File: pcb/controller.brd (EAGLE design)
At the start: 45 x 45 mm, 22 parts, among them U1 74HCT165TSSOP16

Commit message: update resistor values
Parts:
- C1: value (none) -> 100n
- R1, R2, R3, R4, R5, R6, R7, R8: value (none) -> 4.7k
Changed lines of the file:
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@@
 <attribute name="VALUE" x="32.824" y="0.605" size="0.6096" layer="27" font="vector" ratio="20" rot="R90" align="top-left"/>
 </element>
-<element name="R1" library="rcl" library_urn="urn:adsk.eagle:library:334" package="R0603" package3d_urn="urn:adsk.eagle:package:23555/3" value="" x="32.5" y="42.5" smashed="yes" rot="R45">
+<element name="R1" library="rcl" library_urn="urn:adsk.eagle:library:334" package="R0603" package3d_urn="urn:adsk.eagle:package:23555/3" value="4.7k" x="32.5" y="42.5" smashed="yes" rot="R45">
 <attribute name="NAME" x="31.601971875" y="42.5" size="0.6096" layer="25" rot="R45"/>
 <attribute name="POPULARITY" value="77" x="87.279559375" y="38.009871875" size="1.778" layer="27" rot="R45" display="off"/>
@@
 <attribute name="VALUE" x="33.398025" y="40.703946875" size="1.27" layer="27" rot="R45"/>
 </element>
-<element name="R2" library="rcl" library_urn="urn:adsk.eagle:library:334" package="R0603" package3d_urn="urn:adsk.eagle:package:23555/3" value="" x="25" y="42.5" smashed="yes" rot="R45">
+<element name="R2" library="rcl" library_urn="urn:adsk.eagle:library:334" package="R0603" package3d_urn="urn:adsk.eagle:package:23555/3" value="4.7k" x="25" y="42.5" smashed="yes" rot="R45">
 <attribute name="NAME" x="24.101971875" y="42.5" size="0.6096" layer="25" rot="R45"/>
 <attribute name="POPULARITY" value="77" x="82.4736375" y="40.703946875" size="1.778" layer="27" rot="R45" display="off"/>
@@
 <attribute name="VALUE" x="25.898025" y="40.703946875" size="1.27" layer="27" rot="R45"/>
 </element>
-<element name="R3" library="rcl" library_urn="urn:adsk.eagle:library:334" package="R0603" package3d_urn="urn:adsk.eagle:package:23555/3" value="" x="17.5" y="42.5" smashed="yes" rot="R45">
+<element name="R3" library="rcl" library_urn="urn:adsk.eagle:library:334" package="R0603" package3d_urn="urn:adsk.eagle:package:23555/3" value="4.7k" x="17.5" y="42.5" smashed="yes" rot="R45">
 <attribute name="NAME" x="16.601971875" y="42.5" size="0.6096" layer="25" rot="R45"/>
 <attribute name="POPULARITY" value="77" x="77.667715625" y="43.398025" size="1.778" layer="27" rot="R45" display="off"/>
@@
 <attribute name="VALUE" x="18.398025" y="40.703946875" size="1.27" layer="27" rot="R45"/>
 </element>
-<element name="R4" library="rcl" library_urn="urn:adsk.eagle:library:334" package="R0603" package3d_urn="urn:adsk.eagle:package:23555/3" value="" x="10" y="42.5" smashed="yes" rot="R45">
+<element name="R4" library="rcl" library_urn="urn:adsk.eagle:library:334" package="R0603" package3d_urn="urn:adsk.eagle:package:23555/3" value="4.7k" x="10" y="42.5" smashed="yes" rot="R45">
 <attribute name="NAME" x="9.101971875" y="42.5" size="0.6096" layer="25" rot="R45"/>
 <attribute name="POPULARITY" value="77" x="72.861790625" y="46.0921" size="1.778" layer="27" rot="R45" display="off"/>
@@
 <attribute name="VALUE" x="10.898025" y="40.703946875" size="1.27" layer="27" rot="R45"/>
 </element>
-<element name="R5" library="rcl" library_urn="urn:adsk.eagle:library:334" package="R0603" package3d_urn="urn:adsk.eagle:package:23555/3" value="" x="10" y="27.5" smashed="yes" rot="R45">
+<element name="R5" library="rcl" library_urn="urn:adsk.eagle:library:334" package="R0603" package3d_urn="urn:adsk.eagle:package:23555/3" value="4.7k" x="10" y="27.5" smashed="yes" rot="R45">
 <attribute name="NAME" x="9.101971875" y="27.5" size="0.6096" layer="25" rot="R45"/>
 <attribute name="POPULARITY" value="77" x="75.55586875" y="33.786178125" size="1.778" layer="27" rot="R45" display="off"/>
@@
 <attribute name="VALUE" x="10.898025" y="25.703946875" size="1.27" layer="27" rot="R45"/>
 </element>
-<element name="R6" library="rcl" library_urn="urn:adsk.eagle:library:334" package="R0603" package3d_urn="urn:adsk.eagle:package:23555/3" value="" x="17.5" y="27.5" smashed="yes" rot="R45">
+<element name="R6" library="rcl" library_urn="urn:adsk.eagle:library:334" package="R0603" package3d_urn="urn:adsk.eagle:package:23555/3" value="4.7k" x="17.5" y="27.5" smashed="yes" rot="R45">
 <attribute name="NAME" x="16.601971875" y="27.5" size="0.6096" layer="25" rot="R45"/>
 <attribute name="POPULARITY" value="77" x="62.401278125" y="4.15133125" size="1.778" layer="27" rot="R45" display="off"/>
@@
 <attribute name="VALUE" x="18.398025" y="25.703946875" size="1.27" layer="27" rot="R45"/>
 </element>
-<element name="R7" library="rcl" library_urn="urn:adsk.eagle:library:334" package="R0603" package3d_urn="urn:adsk.eagle:package:23555/3" value="" x="25" y="27.5" smashed="yes" rot="R45">
+<element name="R7" library="rcl" library_urn="urn:adsk.eagle:library:334" package="R0603" package3d_urn="urn:adsk.eagle:package:23555/3" value="4.7k" x="25" y="27.5" smashed="yes" rot="R45">
 <attribute name="NAME" x="24.101971875" y="27.5" size="0.6096" layer="25" rot="R45"/>
 <attribute name="POPULARITY" value="77" x="72.59535625" y="6.845409375" size="1.778" layer="27" rot="R45" display="off"/>
@@
 <attribute name="VALUE" x="25.898025" y="25.703946875" size="1.27" layer="27" rot="R45"/>
 </element>
-<element name="R8" library="rcl" library_urn="urn:adsk.eagle:library:334" package="R0603" package3d_urn="urn:adsk.eagle:package:23555/3" value="" x="32.5" y="27.5" smashed="yes" rot="R45">
+<element name="R8" library="rcl" library_urn="urn:adsk.eagle:library:334" package="R0603" package3d_urn="urn:adsk.eagle:package:23555/3" value="4.7k" x="32.5" y="27.5" smashed="yes" rot="R45">
 <attribute name="NAME" x="31.601971875" y="27.5" size="0.6096" layer="25" rot="R45"/>
 <attribute name="POPULARITY" value="77" x="82.78943125" y="9.5394875" size="1.778" layer="27" rot="R45" display="off"/>
@@
 </element>
 <element name="U$2" library="josh" package="JST-ZH-5-SMD-RA" value="JST-ZH-5SMD-RA" x="7.5" y="4.375" smashed="yes" rot="R180"/>
-<element name="C1" library="rcl" library_urn="urn:adsk.eagle:library:334" package="C0603" package3d_urn="urn:adsk.eagle:package:23616/2" value="" x="19.375" y="13.75" smashed="yes" rot="R180">
+<element name="C1" library="rcl" library_urn="urn:adsk.eagle:library:334" package="C0603" package3d_urn="urn:adsk.eagle:package:23616/2" value="100n" x="19.375" y="13.75" smashed="yes" rot="R180">
 <attribute name="NAME" x="23.135" y="14.365" size="0.6096" layer="25" rot="R180"/>
 <attribute name="POPULARITY" value="73" x="19.375" y="13.75" size="1.778" layer="27" rot="R180" display="off"/>

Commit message: update values and name placement
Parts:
- renumbered U$2 to J2
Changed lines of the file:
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@@
 <attribute name="NAME" x="15" y="5.1174" size="0.6096" layer="25" align="bottom-center"/>
 </element>
-<element name="U$2" library="josh" package="JST-ZH-5-SMD-RA" value="JST-ZH-5SMD-RA" x="7.5" y="4.375" smashed="yes" rot="R180"/>
+<element name="J2" library="josh" package="JST-ZH-5-SMD-RA" value="JST-ZH-5SMD-RA" x="7.5" y="4.375" smashed="yes" rot="R180"/>
 <element name="C1" library="rcl" library_urn="urn:adsk.eagle:library:334" package="C0603" package3d_urn="urn:adsk.eagle:package:23616/2" value="100n" x="19.375" y="13.75" smashed="yes" rot="R180">
 <attribute name="NAME" x="23.135" y="14.365" size="0.6096" layer="25" rot="R180"/>
@@
 <signal name="+5V">
 <contactref element="J1" pad="VBUS"/>
-<contactref element="U$2" pad="P$1"/>
+<contactref element="J2" pad="P$1"/>
 <contactref element="R1" pad="2"/>
 <contactref element="R8" pad="2"/>
@@
 <contactref element="J1" pad="SHIELD3"/>
 <contactref element="J1" pad="GND"/>
-<contactref element="U$2" pad="P$5"/>
+<contactref element="J2" pad="P$5"/>
 <contactref element="U1" pad="15"/>
 <contactref element="U1" pad="8"/>
@@
 </signal>
 <signal name="N$1">
-<contactref element="U$2" pad="P$4"/>
+<contactref element="J2" pad="P$4"/>
 <contactref element="U1" pad="2"/>
 <wire x1="9" y1="5.875" x2="9" y2="9.085" width="0.1524" layer="1"/>
@@
 </signal>
 <signal name="N$2">
-<contactref element="U$2" pad="P$3"/>
+<contactref element="J2" pad="P$3"/>
 <contactref element="U1" pad="1"/>
 <wire x1="7.5" y1="5.875" x2="7.5" y2="9.735" width="0.1524" layer="1"/>
@@
 </signal>
 <signal name="N$3">
-<contactref element="U$2" pad="P$2"/>
+<contactref element="J2" pad="P$2"/>
 <contactref element="U1" pad="7"/>
 <wire x1="6" y1="5.875" x2="6" y2="4.3125" width="0.1524" layer="1"/>

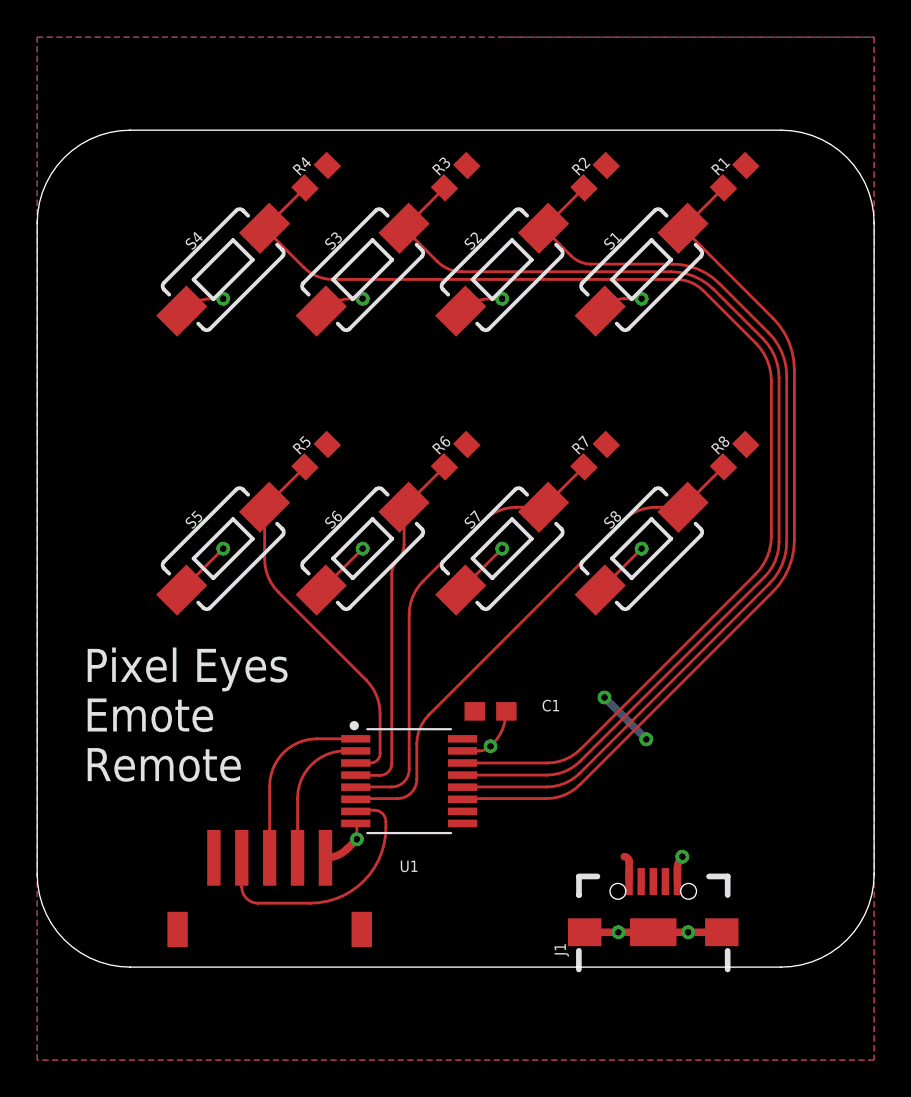
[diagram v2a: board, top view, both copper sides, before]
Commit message: touch up silkscreen and traces
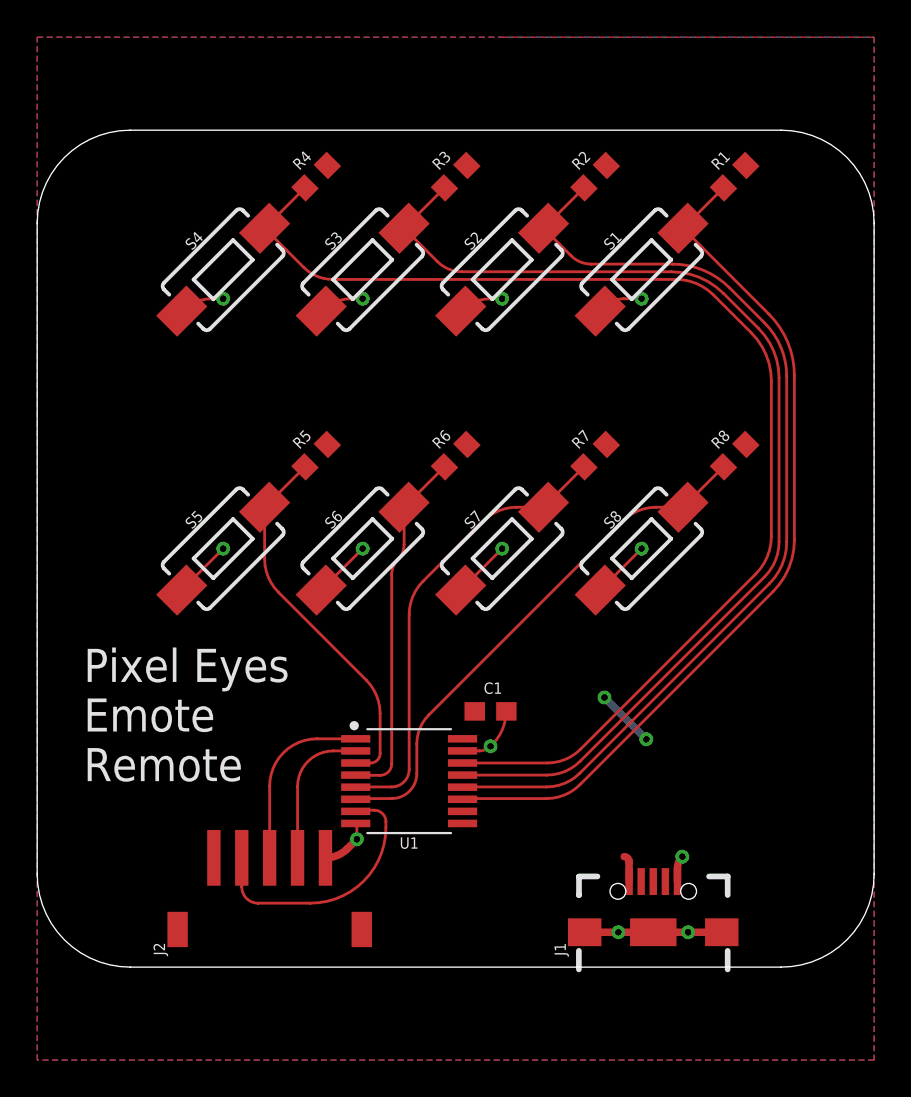
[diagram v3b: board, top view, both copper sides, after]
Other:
- board text added: "J2"
- board text added: "github.com/joshuaboud/pixel_eyes"
